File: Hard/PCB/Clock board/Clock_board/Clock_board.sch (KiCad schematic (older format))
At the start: 19 parts, among them J1 Conn_01x01, J2 Conn_01x01, J3 Conn_01x01, J4 Conn_01x01, J5 Conn_01x01, J6 Conn_01x01, M1 motor, Q1 SI2302, Q2 SI2302, SW1 SW_DPDT_x2

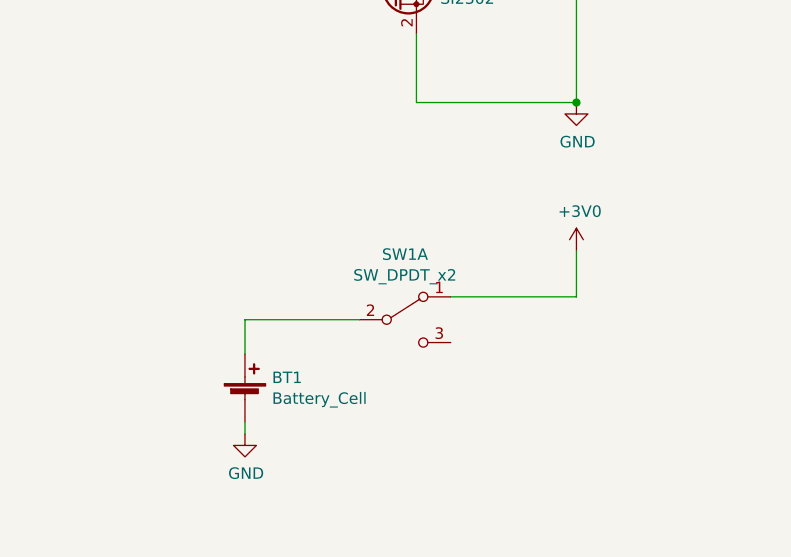
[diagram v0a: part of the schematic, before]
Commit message: shlyeha added switch component to mechanical library, changed scheme switch connection, finished pcb project
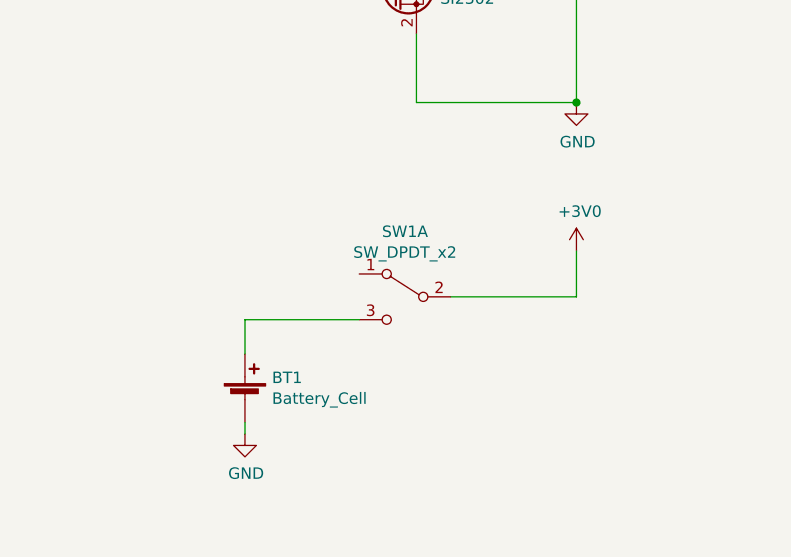
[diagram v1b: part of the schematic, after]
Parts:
- SW1: footprint (none) -> mechanical:switch_ms-22c01
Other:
- moved on the sheet: SW1A
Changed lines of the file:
@@
 L Switch:SW_DPDT_x2 SW1
 U 1 1 60D1FC06
-P 8850 4750
-F 0 "SW1" H 8850 5035 50  0000 C CNN
-F 1 "SW_DPDT_x2" H 8850 4944 50  0000 C CNN
-F 2 "" H 8850 4750 50  0001 C CNN
-F 3 "~" H 8850 4750 50  0001 C CNN
-	1    8850 4750
-	1    0    0    -1
+P 8850 4650
+F 0 "SW1" H 8850 4935 50  0000 C CNN
+F 1 "SW_DPDT_x2" H 8850 4844 50  0000 C CNN
+F 2 "mechanical:switch_ms-22c01" H 8850 4650 50  0001 C CNN
+F 3 "~" H 8850 4650 50  0001 C CNN
+	1    8850 4650
+	-1   0    0    -1
 $EndComp
 Wire Wire Line

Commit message: shlyeha added Details.txt file, defined components fields
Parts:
- BT1: value Battery_Cell -> MY-2032-06; Description (none) -> DIP Battery Accessories/Contacts/Springs RoHS; Item # (none) -> 11; Manufacturer (none) -> MYOUNG; Note (none) -> (none); Package (none) -> DIP; Type (none) -> thru-hole
- C1: Description (none) -> 100nF ±10% 16V X7R 0402 Multilayer Ceramic Capacitors MLCC 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; Item # (none) -> 1; Manufacturer (none) -> YAGEO; Package (none) -> C0402; Type (none) -> SMD
- C2: Description (none) -> 1uF ±10% 6.3V X7R 0402 Multilayer Ceramic Capacitors MLCC -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; Item # (none) -> 2; Manufacturer (none) -> Samsung Electro-Mechanics; Package (none) -> C0402; Type (none) -> SMD
- D1: value BAT54C, 215 -> BAT54C,215; Description (none) -> 30V 200mA 800mV @ 100mA SOT-23(SOT-23-3) Schottky Barrier D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; Item # (none) -> 3; Manufacturer (none) -> Nexperia; Package (none) -> SOT-23(SOT-23-3); Type (none) -> SMD
- DD1: Description (none) -> TSSOP-20 ST Microelectronics RoHS; Item # (none) -> 4; Manufacturer (none) -> STMicroelectronics; Package (none) -> TSSOP-20; Type (none) -> SMD
- J1, J2, J3, J4, J5, J6: Manufacturer (none) -> asd; Note (none) -> note
- Q1, Q2: Description (none) -> N-Channel 20V 2.1A 1.2V @ 50uA 72mΩ @ 3.6A,4.5V 400mW SOT-2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; Item # (none) -> 5; Manufacturer (none) -> Guangdong Hottech; Package (none) -> SOT-23(SOT-23-3); Type (none) -> SMD
- R1: Description (none) -> 10kΩ ±5% 1/16W ±100ppm/℃ 0402 Chip Resistor - Surface Mount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; Item # (none) -> 6; Manufacturer (none) -> YAGEO; Package (none) -> R0402; Type (none) -> SMD
- R2: Description (none) -> 510Ω ±5% 0.125W ±100ppm/℃ 0805 Chip Resistor - Surface Moun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; Item # (none) -> 7; Manufacturer (none) -> UNI-ROYAL(Uniroyal Elec); Package (none) -> R0805; Type (none) -> SMD
- R3: Description (none) -> 200Ω ±1% 0.125W ±200ppm/℃ 0805 Chip Resistor - Surface Moun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; Item # (none) -> 8; Manufacturer (none) -> ROHM Semicon; Package (none) -> R0805; Type (none) -> SMD
- R4: Description (none) -> 10MΩ ±1% 0.125W 0805 Chip Resistor - Surface Mount RoHS; Item # (none) -> 9; Manufacturer (none) -> TyoHM; Package (none) -> R0805; Type (none) -> SMD
- SW1: value SW_DPDT_x2 -> MS-22C01-G010; Description (none) -> SMD,7.2x3.5x2.5mm Toggle Switches RoHS; Item # (none) -> 10; Manufacturer (none) -> G-Switch; Package (none) -> SMD,7.2x3.5x2.5mm; Type (none) -> SMD
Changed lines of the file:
@@
 F 2 "Package_TO_SOT_SMD:SOT-23" H 9000 3225 50  0001 L CIN
 F 3 "https://www.taiwansemi.com/products/datasheet/TSM2302CX_E1608.pdf" H 8800 3300 50  0001 L CNN
+F 4 "5" H 8800 3300 50  0001 C CNN "Item #"
+F 5 "N-Channel 20V 2.1A 1.2V @ 50uA 72mΩ @ 3.6A,4.5V 400mW SOT-23(SOT-23-3) MOSFETs RoHS" H 8800 3300 50  0001 C CNN "Description"
+F 6 "Guangdong Hottech" H 8800 3300 50  0001 C CNN "Manufacturer"
+F 7 "SOT-23(SOT-23-3)" H 8800 3300 50  0001 C CNN "Package"
+F 8 "SMD" H 8800 3300 50  0001 C CNN "Type"
 	1    8800 3300
 	1    0    0    -1
@@
 F 2 "Package_TO_SOT_SMD:SOT-23" H 9700 2725 50  0001 L CIN
 F 3 "https://www.taiwansemi.com/products/datasheet/TSM2302CX_E1608.pdf" H 9500 2800 50  0001 L CNN
+F 4 "5" H 9500 2800 50  0001 C CNN "Item #"
+F 5 "N-Channel 20V 2.1A 1.2V @ 50uA 72mΩ @ 3.6A,4.5V 400mW SOT-23(SOT-23-3) MOSFETs RoHS" H 9500 2800 50  0001 C CNN "Description"
+F 6 "Guangdong Hottech" H 9500 2800 50  0001 C CNN "Manufacturer"
+F 7 "SOT-23(SOT-23-3)" H 9500 2800 50  0001 C CNN "Package"
+F 8 "SMD" H 9500 2800 50  0001 C CNN "Type"
 	1    9500 2800
 	1    0    0    -1
@@
 F 2 "Resistor_SMD:R_0805_2012Metric" H 8900 2200 50  0001 C CNN
 F 3 "~" H 8900 2200 50  0001 C CNN
+F 4 "9" H 8900 2200 50  0001 C CNN "Item #"
+F 5 "10MΩ ±1% 0.125W 0805 Chip Resistor - Surface Mount RoHS" H 8900 2200 50  0001 C CNN "Description"
+F 6 "TyoHM" H 8900 2200 50  0001 C CNN "Manufacturer"
+F 7 "R0805" H 8900 2200 50  0001 C CNN "Package"
+F 8 "SMD" H 8900 2200 50  0001 C CNN "Type"
 	1    8900 2200
 	1    0    0    -1
@@
 F 2 "Resistor_SMD:R_0805_2012Metric" H 8400 3300 50  0001 C CNN
 F 3 "~" H 8400 3300 50  0001 C CNN
+F 4 "8" H 8400 3300 50  0001 C CNN "Item #"
+F 5 "200Ω ±1% 0.125W ±200ppm/℃ 0805 Chip Resistor - Surface Mount RoHS" H 8400 3300 50  0001 C CNN "Description"
+F 6 "ROHM Semicon" H 8400 3300 50  0001 C CNN "Manufacturer"
+F 7 "R0805" H 8400 3300 50  0001 C CNN "Package"
+F 8 "SMD" H 8400 3300 50  0001 C CNN "Type"
 	1    8400 3300
 	0    1    1    0
@@
 F 2 "Package_SO:TSSOP-20_4.4x6.5mm_P0.65mm" H 4750 4850 50  0001 C CNN
 F 3 "" H 4750 4850 50  0001 C CNN
+F 4 "4" H 4750 4850 50  0001 C CNN "Item #"
+F 5 "TSSOP-20 ST Microelectronics RoHS" H 4750 4850 50  0001 C CNN "Description"
+F 6 "STMicroelectronics" H 4750 4850 50  0001 C CNN "Manufacturer"
+F 7 "TSSOP-20" H 4750 4850 50  0001 C CNN "Package"
+F 8 "SMD" H 4750 4850 50  0001 C CNN "Type"
 	1    4750 4850
 	1    0    0    -1
@@
 P 9600 2200
 F 0 "D1" V 9600 2288 50  0000 L CNN
-F 1 "BAT54C, 215" V 9555 2287 50  0001 L CNN
+F 1 "BAT54C,215" V 9555 2287 50  0001 L CNN
 F 2 "Package_TO_SOT_SMD:SOT-23" H 9675 2325 50  0001 L CNN
 F 3 "http://www.diodes.com/_files/datasheets/ds11005.pdf" H 9520 2200 50  0001 C CNN
+F 4 "3" H 9600 2200 50  0001 C CNN "Item #"
+F 5 "30V 200mA 800mV @ 100mA SOT-23(SOT-23-3) Schottky Barrier Diodes (SBD) RoHS" H 9600 2200 50  0001 C CNN "Description"
+F 6 "Nexperia" H 9600 2200 50  0001 C CNN "Manufacturer"
+F 7 "SOT-23(SOT-23-3)" H 9600 2200 50  0001 C CNN "Package"
+F 8 "SMD" H 9600 2200 50  0001 C CNN "Type"
 	1    9600 2200
 	0    -1   -1   0
@@
 F 2 "Resistor_SMD:R_0402_1005Metric" H 3300 4350 50  0001 C CNN
 F 3 "~" H 3300 4350 50  0001 C CNN
+F 4 "6" H 3300 4350 50  0001 C CNN "Item #"
+F 5 "10kΩ ±5% 1/16W ±100ppm/℃ 0402 Chip Resistor - Surface Mount RoHS" H 3300 4350 50  0001 C CNN "Description"
+F 6 "YAGEO" H 3300 4350 50  0001 C CNN "Manufacturer"
+F 7 "R0402" H 3300 4350 50  0001 C CNN "Package"
+F 8 "SMD" H 3300 4350 50  0001 C CNN "Type"
 	1    3300 4350
 	1    0    0    -1
@@
 F 2 "Resistor_SMD:R_0805_2012Metric" H 6050 4150 50  0001 C CNN
 F 3 "~" H 6050 4150 50  0001 C CNN
+F 4 "7" H 6050 4150 50  0001 C CNN "Item #"
+F 5 "510Ω ±5% 0.125W ±100ppm/℃ 0805 Chip Resistor - Surface Mount RoHS" H 6050 4150 50  0001 C CNN "Description"
+F 6 "UNI-ROYAL(Uniroyal Elec)" H 6050 4150 50  0001 C CNN "Manufacturer"
+F 7 "R0805" H 6050 4150 50  0001 C CNN "Package"
+F 8 "SMD" H 6050 4150 50  0001 C CNN "Type"
 	1    6050 4150
 	1    0    0    1
@@
 F 2 "connector:custom_connector" H 4500 2600 50  0001 C CNN
 F 3 "~" H 4500 2600 50  0001 C CNN
+F 4 "asd" H 4500 2600 50  0001 C CNN "Manufacturer"
+F 5 "note" H 4500 2600 50  0001 C CNN "Note"
 	1    4500 2600
 	-1   0    0    -1
@@
 F 2 "connector:custom_connector" H 4500 2700 50  0001 C CNN
 F 3 "~" H 4500 2700 50  0001 C CNN
+F 4 "asd" H 4500 2700 50  0001 C CNN "Manufacturer"
+F 5 "note" H 4500 2700 50  0001 C CNN "Note"
 	1    4500 2700
 	-1   0    0    -1
@@
 F 2 "connector:custom_connector" H 4500 2800 50  0001 C CNN
 F 3 "~" H 4500 2800 50  0001 C CNN
+F 4 "asd" H 4500 2800 50  0001 C CNN "Manufacturer"
+F 5 "note" H 4500 2800 50  0001 C CNN "Note"
 	1    4500 2800
 	-1   0    0    -1
@@
 F 2 "connector:custom_connector" H 4500 2900 50  0001 C CNN
 F 3 "~" H 4500 2900 50  0001 C CNN
+F 4 "asd" H 4500 2900 50  0001 C CNN "Manufacturer"
+F 5 "note" H 4500 2900 50  0001 C CNN "Note"
 	1    4500 2900
 	-1   0    0    -1
@@
 F 2 "connector:custom_connector" H 4500 3000 50  0001 C CNN
 F 3 "~" H 4500 3000 50  0001 C CNN
+F 4 "asd" H 4500 3000 50  0001 C CNN "Manufacturer"
+F 5 "note" H 4500 3000 50  0001 C CNN "Note"
 	1    4500 3000
 	-1   0    0    -1
@@
 F 2 "connector:custom_connector" H 4500 3100 50  0001 C CNN
 F 3 "~" H 4500 3100 50  0001 C CNN
+F 4 "asd" H 4500 3100 50  0001 C CNN "Manufacturer"
+F 5 "note" H 4500 3100 50  0001 C CNN "Note"
 	1    4500 3100
 	-1   0    0    -1
@@
 P 8150 5100
 F 0 "BT1" H 8268 5196 50  0000 L CNN
-F 1 "Battery_Cell" H 8268 5105 50  0000 L CNN
+F 1 "MY-2032-06" H 8268 5105 50  0000 L CNN
 F 2 "mechanical:cr2032_holder" V 8150 5160 50  0001 C CNN
 F 3 "~" V 8150 5160 50  0001 C CNN
+F 4 "11" H 8150 5100 50  0001 C CNN "Item #"
+F 5 " " H 8150 5100 50  0001 C CNN "Note"
+F 6 "thru-hole" H 8150 5100 50  0001 C CNN "Type"
+F 7 "DIP Battery Accessories/Contacts/Springs RoHS" H 8150 5100 50  0001 C CNN "Description"
+F 8 "MYOUNG" H 8150 5100 50  0001 C CNN "Manufacturer"
+F 9 "DIP" H 8150 5100 50  0001 C CNN "Package"
 	1    8150 5100
 	1    0    0    -1
@@
 P 8850 4650
 F 0 "SW1" H 8850 4935 50  0000 C CNN
-F 1 "SW_DPDT_x2" H 8850 4844 50  0000 C CNN
+F 1 "MS-22C01-G010" H 8850 4844 50  0000 C CNN
 F 2 "mechanical:switch_ms-22c01" H 8850 4650 50  0001 C CNN
 F 3 "~" H 8850 4650 50  0001 C CNN
+F 4 "10" H 8850 4650 50  0001 C CNN "Item #"
+F 5 "SMD,7.2x3.5x2.5mm Toggle Switches RoHS" H 8850 4650 50  0001 C CNN "Description"
+F 6 "G-Switch" H 8850 4650 50  0001 C CNN "Manufacturer"
+F 7 "SMD,7.2x3.5x2.5mm" H 8850 4650 50  0001 C CNN "Package"
+F 8 "SMD" H 8850 4650 50  0001 C CNN "Type"
 	1    8850 4650
 	-1   0    0    -1
@@
 F 2 "Capacitor_SMD:C_0402_1005Metric" H 2800 4900 50  0001 C CNN
 F 3 "~" H 2800 4900 50  0001 C CNN
+F 4 "2" H 2800 4900 50  0001 C CNN "Item #"
+F 5 "1uF ±10% 6.3V X7R 0402 Multilayer Ceramic Capacitors MLCC - SMD/SMT RoHS" H 2800 4900 50  0001 C CNN "Description"
+F 6 "Samsung Electro-Mechanics" H 2800 4900 50  0001 C CNN "Manufacturer"
+F 7 "C0402" H 2800 4900 50  0001 C CNN "Package"
+F 8 "SMD" H 2800 4900 50  0001 C CNN "Type"
 	1    2800 4900
 	1    0    0    -1
@@
 F 2 "Capacitor_SMD:C_0402_1005Metric" H 2500 4900 50  0001 C CNN
 F 3 "~" H 2500 4900 50  0001 C CNN
+F 4 "1" H 2500 4900 50  0001 C CNN "Item #"
+F 5 "100nF ±10% 16V X7R 0402 Multilayer Ceramic Capacitors MLCC - SMD/SMT RoHS" H 2500 4900 50  0001 C CNN "Description"
+F 6 "C0402" H 2500 4900 50  0001 C CNN "Package"
+F 7 "SMD" H 2500 4900 50  0001 C CNN "Type"
+F 8 "YAGEO" H 2500 4900 50  0001 C CNN "Manufacturer"
 	1    2500 4900
 	1    0    0    -1
